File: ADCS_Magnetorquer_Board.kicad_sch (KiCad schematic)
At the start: 17 parts, among them Q1 ZXMP2120FFTA, Q2 ZXMP2120FFTA, U1 LTC4368CMS-1#PBF, U2 INA226AIDGSR

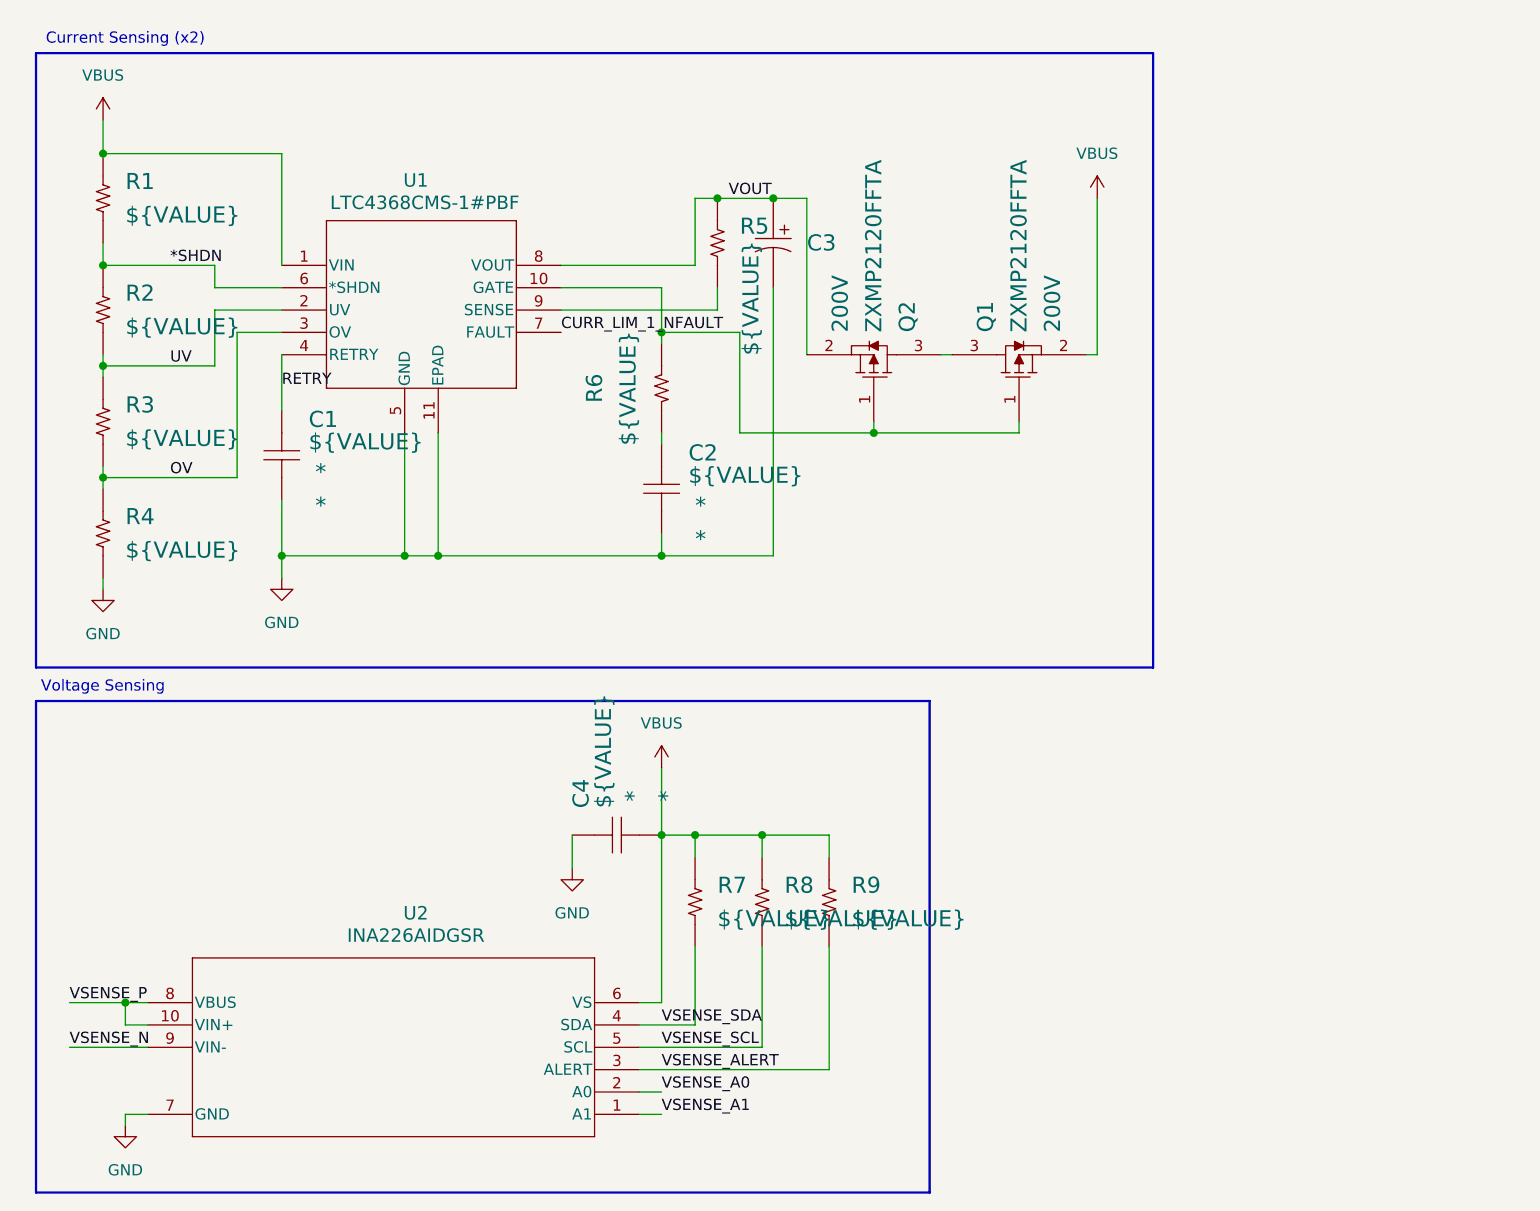
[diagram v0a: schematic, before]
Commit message: Added sub-layers for main schematic sheet.
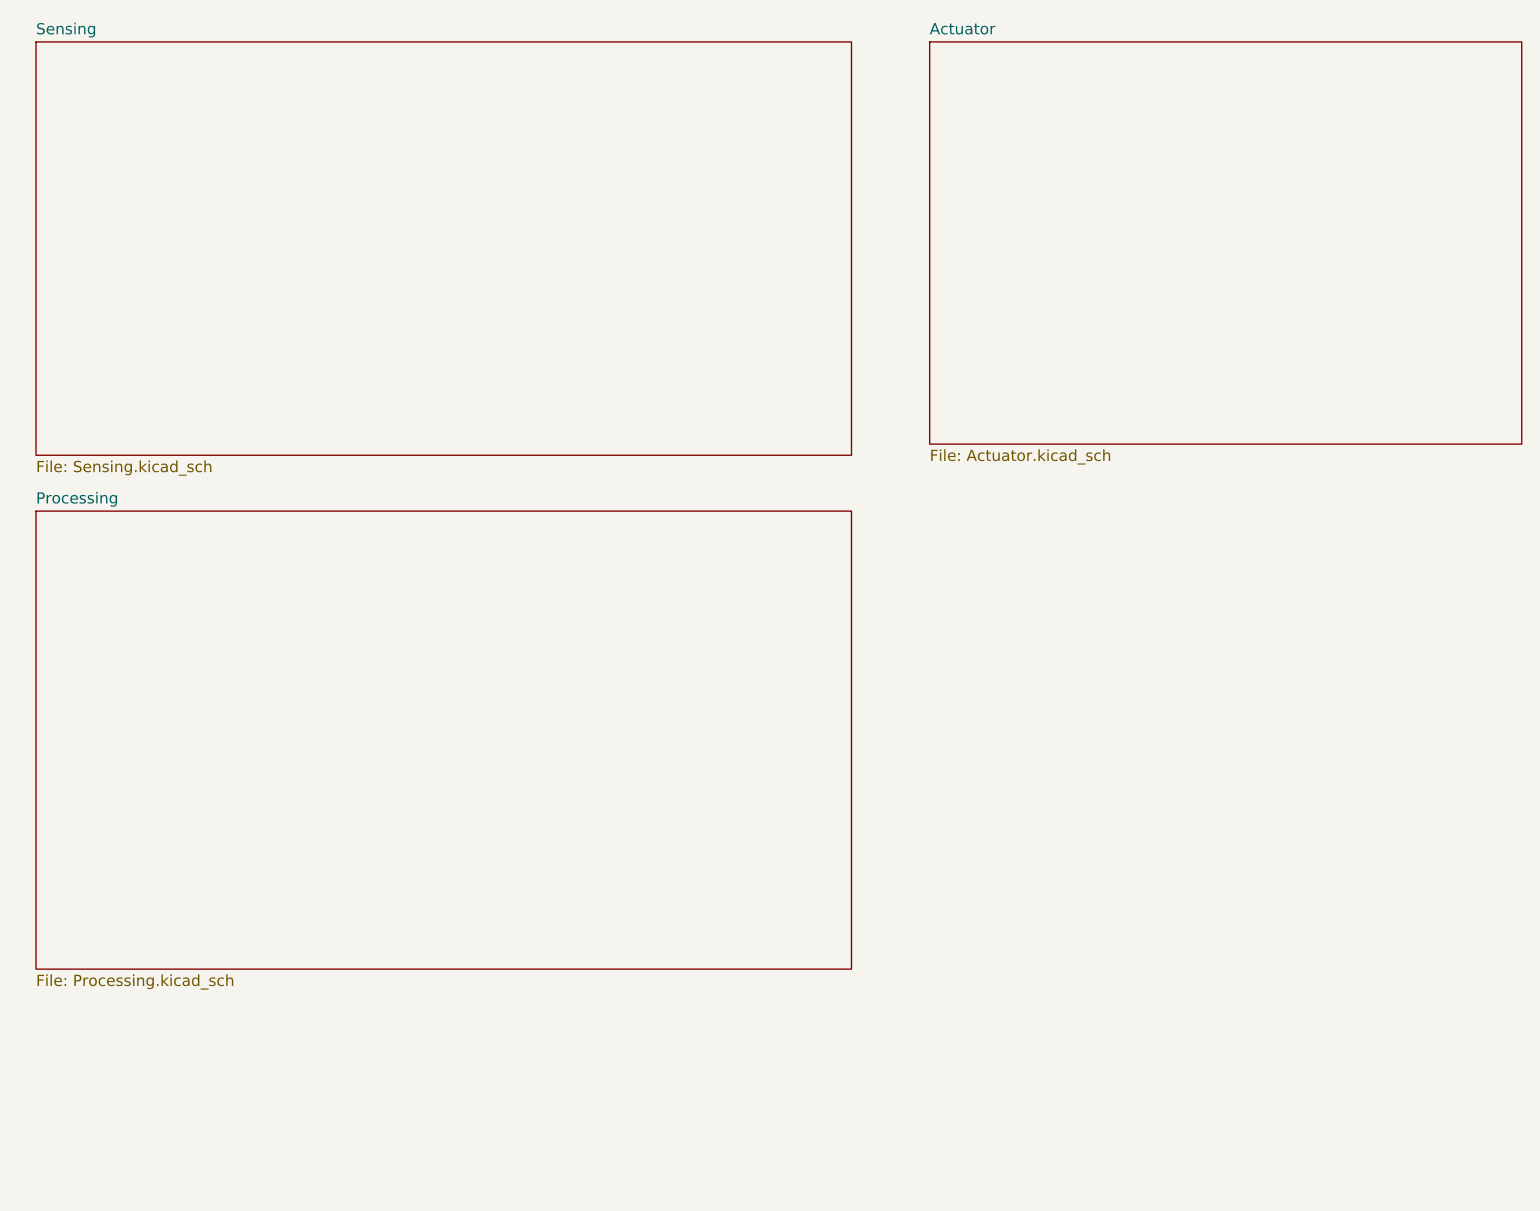
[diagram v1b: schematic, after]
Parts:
- removed C1, C2, C4: ${VALUE}, symbol Capacitor:Capacitor_NP
- removed C3: ${VALUE}, Package_SO:Toshiba_SOIC-4-6_4.4x3.6mm_P1.27mm, symbol Capacitor:Capacitor_POL
- removed Q1, Q2: ZXMP2120FFTA, Other:TRXSOFL3P95_290X240X100L58X40N, symbol DB:Transistor/348
- removed R1, R2, R3, R4, R5, R6, R7, R8, R9: ${VALUE}, Other:DPAK3P508_1229X317L176X89T749X673N, symbol Resistor:Resistor
- removed U1: LTC4368CMS-1#PBF, Leaded:MS_10_ADI, symbol DB:Protection/2607
- removed U2: INA226AIDGSR, Leaded:DGS10, symbol DB:Power/2606
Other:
- added sheet Actuator (Actuator.kicad_sch)
- added sheet Processing (Processing.kicad_sch)
- added sheet Sensing (Sensing.kicad_sch)
- note removed: "Current Sensing (x2)"
- note removed: "Voltage Sensing"
